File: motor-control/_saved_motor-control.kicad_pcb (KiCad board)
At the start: 2 copper layers, 74 parts, among them P1 CONN_02X12, P2 to_motor_phase_1, P3 to_motor_phase_2, P4 to_motor_phase_3, P5 CONN_01X01, P6 CONN_01X01, Q1 CSD19536KTT, Q10 CSD19536KTT, Q11 CSD19536KTT, Q12 CSD19536KTT, Q2 CSD19536KTT, Q3 CSD19536KTT, Q4 CSD19536KTT, Q5 CSD19536KTT, Q6 CSD19536KTT, Q7 CSD19536KTT, Q8 CSD19536KTT, Q9 CSD19536KTT, U1 ACS770, U2 ACS770, U3 ACS770, U4 DRV8301

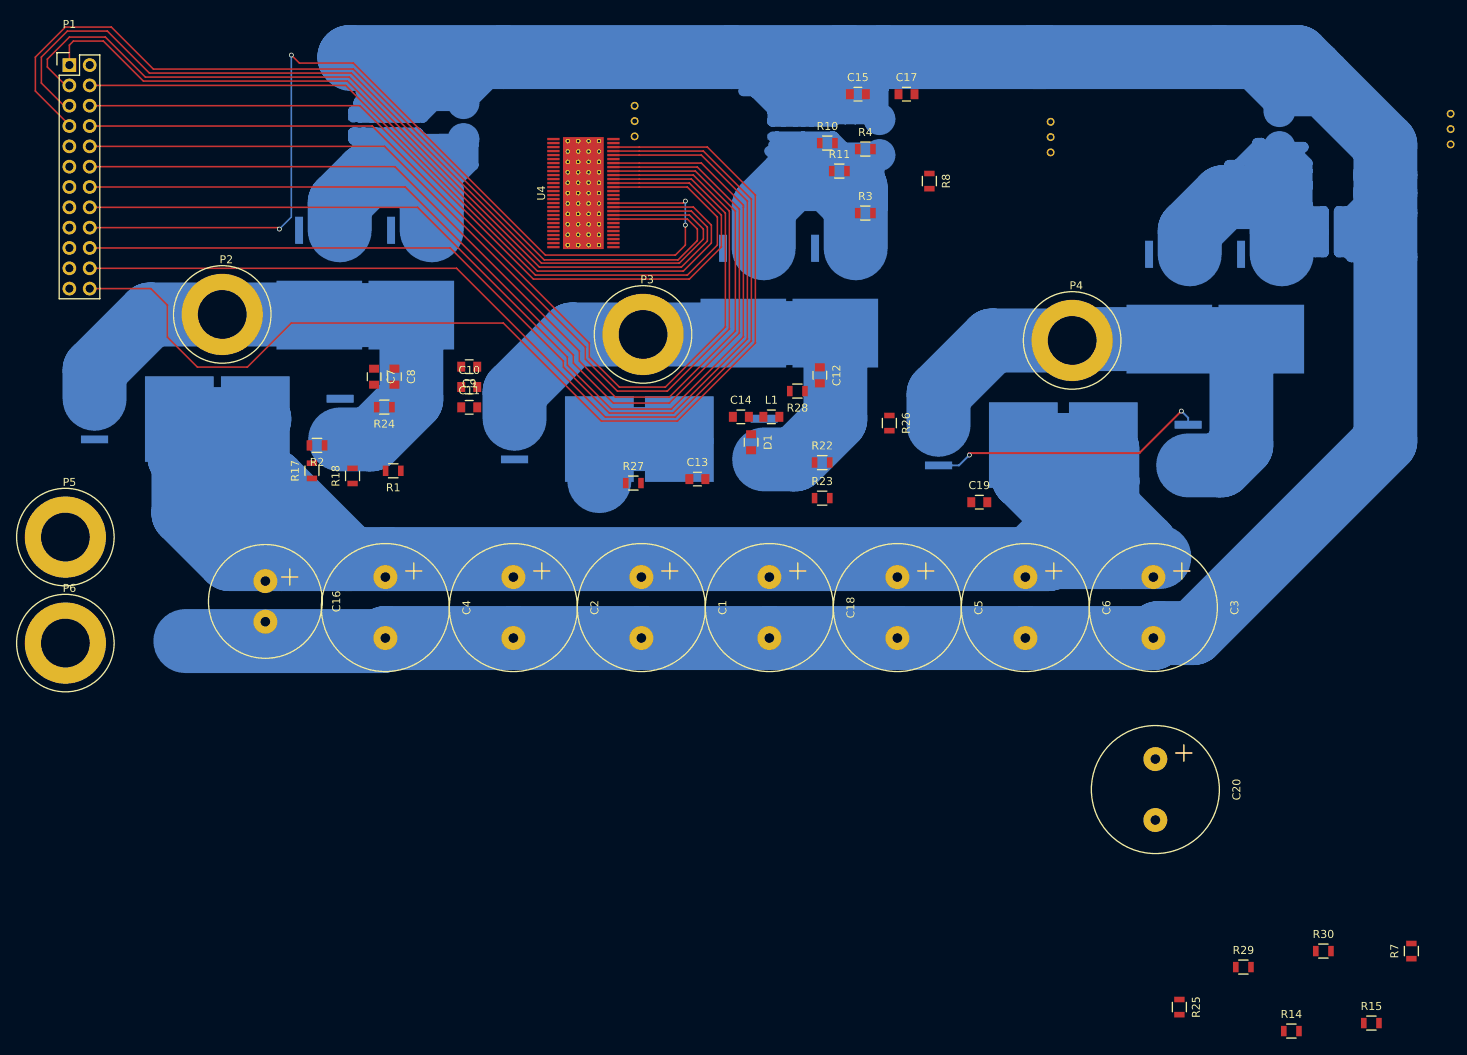
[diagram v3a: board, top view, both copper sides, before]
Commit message: Started using autorouter push-and-shove
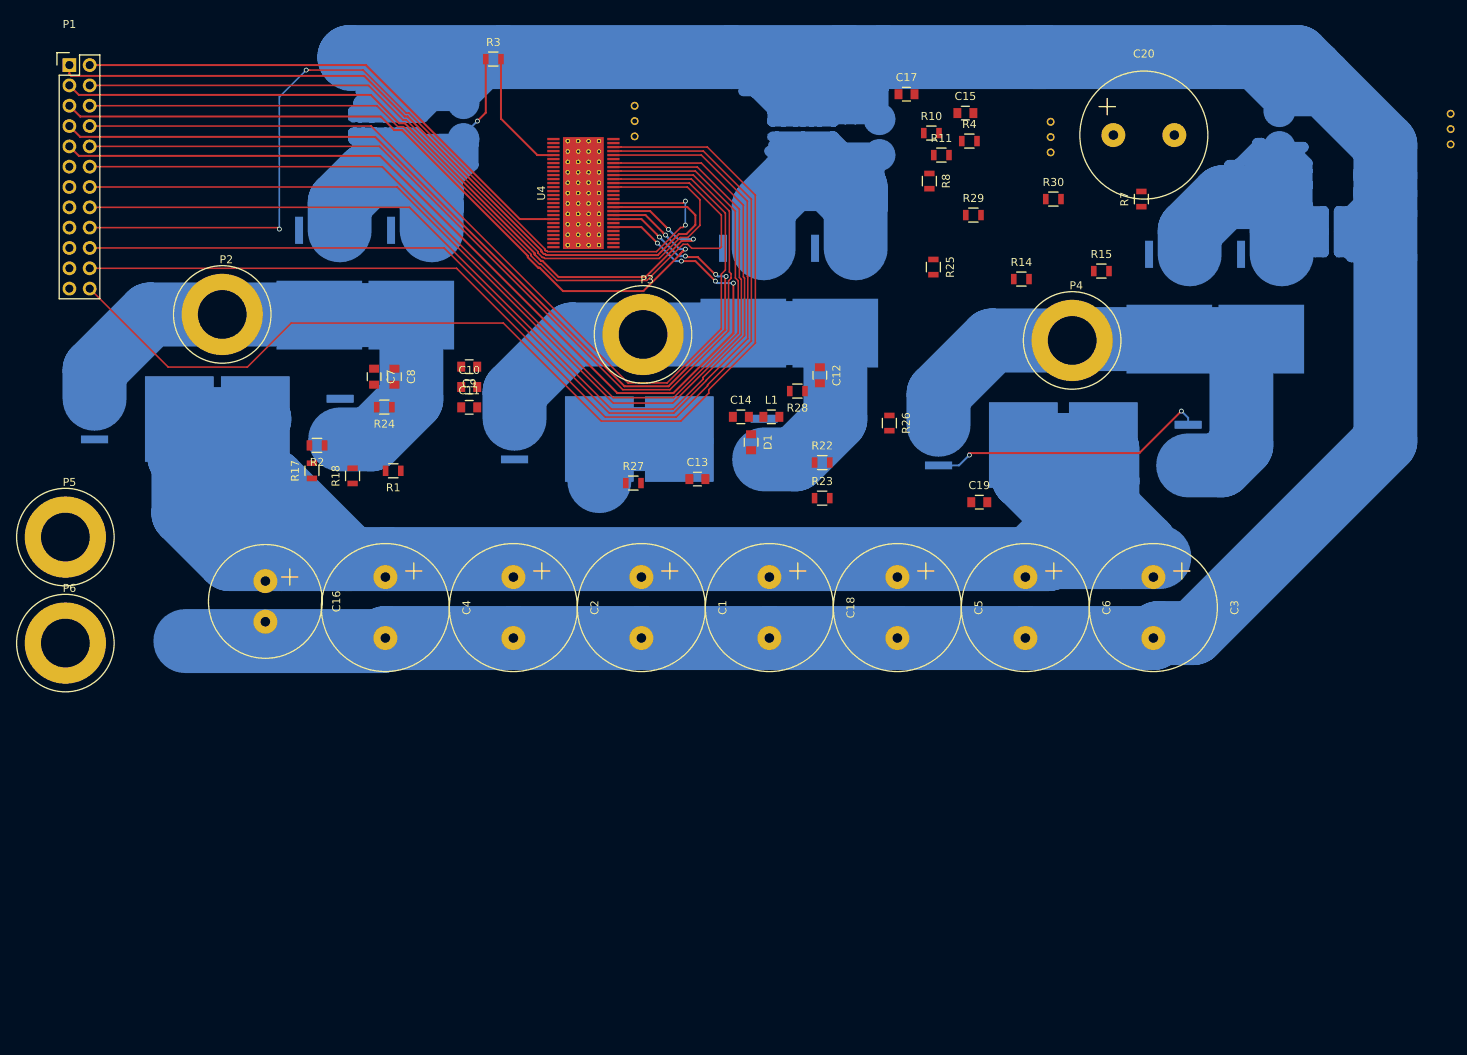
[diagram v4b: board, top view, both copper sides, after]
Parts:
- moved R14 99.9 mm to (138.9, 44.3)
- moved R15 99.9 mm to (148.9, 43.3)
- moved R29 99.9 mm to (132.9, 36.3)
- moved R30 99.9 mm to (142.9, 34.3)
- moved R7 99.9 mm to (153.9, 34.3)
- moved R25 97.5 mm to (127.9, 42.8)
- moved C20 78.2 mm to (150.4, 26.3), turned to 0 degrees
- moved R3 50.3 mm to (72.9, 16.8)
- moved C15 13.6 mm to (131.9, 23.5)
- moved R10 13.1 mm to (127.6, 26.0)
- moved R4 13.0 mm to (132.4, 27.0)
- moved R11 12.9 mm to (128.9, 28.8)
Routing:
- net /Gate-Driver/nFault: track 0.00 -> 123.0 mm, vias 0 -> 4
- net /Gate-Driver/VDD_SPI: track 0.00 -> 65.9 mm
- net /Gate-Driver/SDI: track 118.5 -> 100.3 mm, vias 0 -> 2
- net /Gate-Driver/SN1: track 0.00 -> 15.9 mm
- net /Gate-Driver/SDO: track 115.9 -> 101.9 mm, vias 0 -> 2
- net /Gate-Driver/SL_A: track 149.8 -> 161.0 mm, vias 0 -> 1
- net /Gate-Driver/SCLK: track 111.7 -> 102.3 mm
- net /Gate-Driver/EN_GATE: track 107.9 -> 101.8 mm
- net /Gate-Driver/DC_CAL: track 120.9 -> 115.4 mm
- net /Gate-Driver/nSCS: track 120.2 -> 122.4 mm, vias 0 -> 4
- net /Gate-Driver/S02: track 139.7 -> 137.7 mm
- net /Gate-Driver/INL_A: track 127.1 -> 125.5 mm
- net /Gate-Driver/INH_B: track 127.8 -> 127.1 mm
- net /Gate-Driver/INH_A: track 108.7 -> 109.4 mm

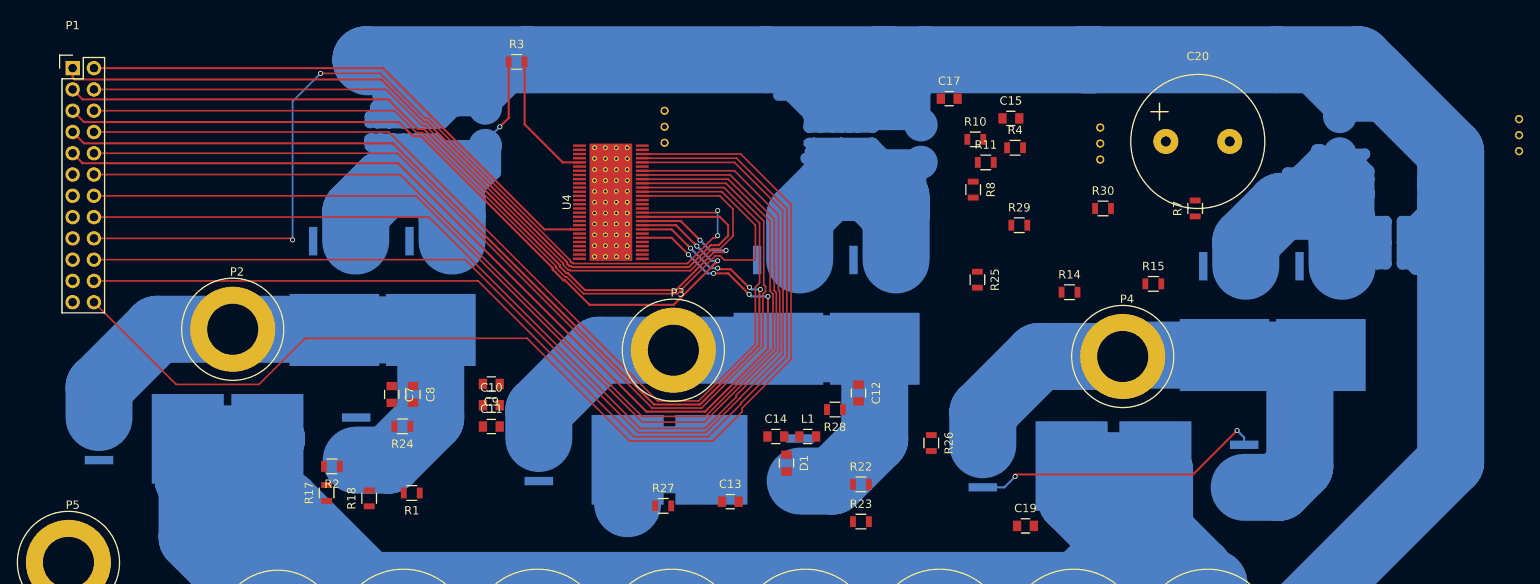
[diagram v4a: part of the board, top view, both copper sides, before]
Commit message: More changes using autorouter.  Finished connector
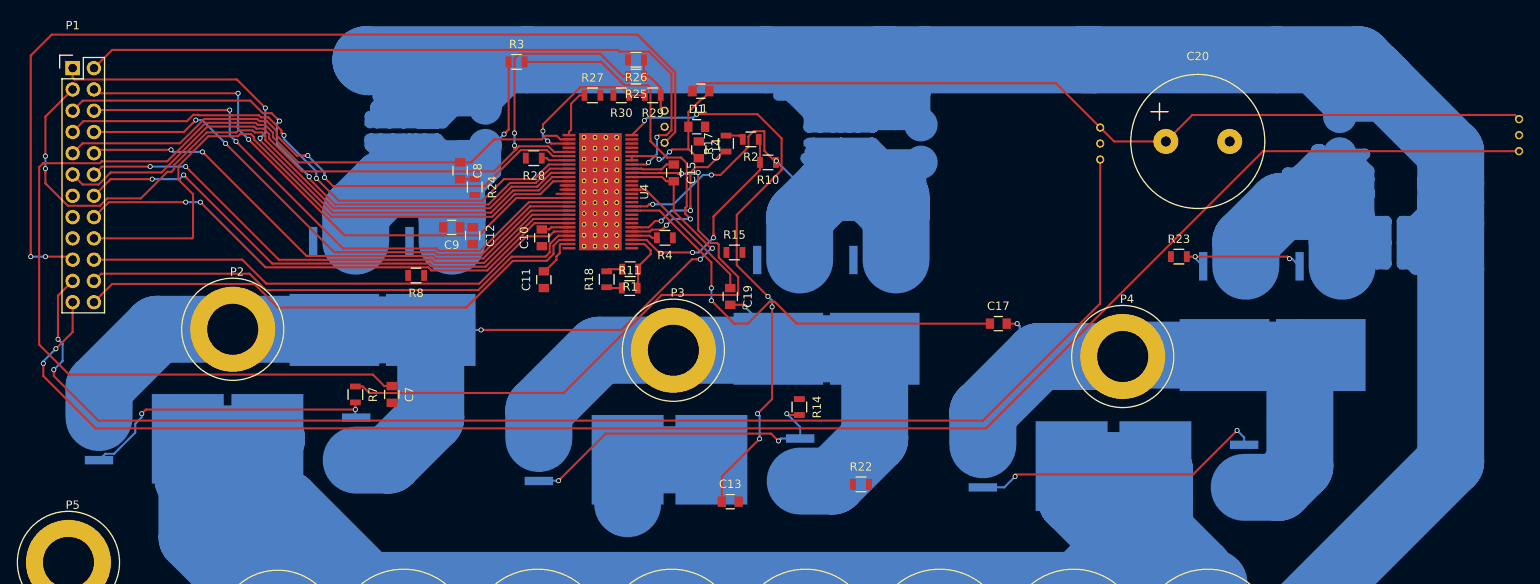
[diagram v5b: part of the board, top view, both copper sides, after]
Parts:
- moved R7 102.7 mm to (53.6, 56.5), turned to 270 degrees
- moved R8 67.3 mm to (60.9, 42.3), turned to 180 degrees
- moved R2 63.4 mm to (100.8, 26.0)
- moved R17 63.4 mm to (97.9, 26.5)
- moved R30 59.1 mm to (85.4, 20.8), turned to 180 degrees
- moved R26 57.8 mm to (87.1, 16.5), turned to 180 degrees
- moved R15 50.1 mm to (98.9, 39.5)
- moved C12 49.7 mm to (67.6, 37.5)
- moved R27 49.7 mm to (81.9, 20.8)
- moved R23 49.4 mm to (151.9, 40.0)
- moved R25 47.4 mm to (87.1, 18.5), turned to 180 degrees
- moved R28 46.8 mm to (74.9, 28.3)
- moved R29 46.4 mm to (89.1, 20.8), turned to 180 degrees
- moved R11 45.1 mm to (86.4, 43.8)
- moved C19 44.6 mm to (98.4, 44.8), turned to 270 degrees
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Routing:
- net /power mosfets & current sensing/hall_3: track 0.00 -> 202.7 mm, vias 0 -> 2
- net /power mosfets & current sensing/hall_2: track 0.00 -> 162.8 mm, vias 0 -> 2
- net Net-(C7-Pad1): track 0.00 -> 134.5 mm
- net /power mosfets & current sensing/hall_1: track 0.00 -> 117.9 mm, vias 0 -> 2
- net VCC: track 0.00 -> 111.7 mm
- net /Gate-Driver/nOCTW: track 0.00 -> 92.5 mm, vias 0 -> 2
- net /Gate-Driver/GH_A: track 0.00 -> 75.9 mm, vias 0 -> 2
- net /Gate-Driver/S02: track 137.7 -> 62.7 mm
- net /Gate-Driver/S01: track 131.9 -> 61.2 mm
- net /Gate-Driver/REF: track 131.0 -> 60.5 mm
- net Net-(C13-Pad1): track 0.00 -> 70.3 mm, vias 0 -> 6
- net /Gate-Driver/INL_C: track 131.1 -> 63.2 mm, vias 0 -> 2
- net /Gate-Driver/INH_C: track 129.9 -> 64.6 mm, vias 0 -> 2
- net /Gate-Driver/INL_B: track 129.1 -> 64.2 mm, vias 0 -> 2
- net /Gate-Driver/INH_B: track 127.1 -> 64.6 mm, vias 0 -> 2
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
